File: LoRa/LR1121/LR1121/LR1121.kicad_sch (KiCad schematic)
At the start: 0 parts

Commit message: [LR1121] Add GPS in the project
GPS and power module was add in the project
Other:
- added sheet LoRa-system (LoRa-system.kicad_sch)
- note added: "Charger battery circuit."
- note added: "LR1121: DIO9, DIO8 Multi-purpose digital I/O STM32L55: PA2 UART2_TX PA3 UART2_RX PA4 SPI1_NSS PA5 SPI1_SCK PA6 SPI1_MISO PA7 SPI1_MOSI PA9 UART1_TX PA10 UART1_RX PA11 USB_DM PA12 USB_DP PB6 I2C1_SCL PB7 I2C1_SDA PB8 CAN1_TX PB9 CAN1_RX PB10 I2C2_SCL PB11 I2C2_SDA PB12 SPI2_NSS PB13 SPI2_SCK PB14 SPI2_MISO PB15 SPI2_MOSI"
- note added: "MT29F4G01ABAFDWB-IT:F TR 133 MHz clock frequency (MAX) LBAA0XV2GT: The SPI runs on the external SCK clock to allow high speed up to 16 MHz"
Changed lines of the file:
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@@
 	(generator_version "9.0")
 	(paper "A4")
+	(text "	LR1121:\nDIO9, DIO8 		Multi-purpose digital I/O\n\n	STM32L55:\n\nPA2		UART2_TX	\nPA3		UART2_RX\n\nPA4		SPI1_NSS\nPA5		SPI1_SCK\nPA6		SPI1_MISO\nPA7		SPI1_MOSI\n\nPA9		UART1_TX\nPA10	UART1_RX\n\nPA11	USB_DM\nPA12	USB_DP\n\nPB6		I2C1_SCL\nPB7		I2C1_SDA\n\nPB8		CAN1_TX\nPB9		CAN1_RX\n\nPB10	I2C2_SCL\nPB11	I2C2_SDA\n\nPB12	SPI2_NSS\nPB13	SPI2_SCK\nPB14	SPI2_MISO\nPB15	SPI2_MOSI"
+		(exclude_from_sim no)
+		(at 18.034 20.574 0)
+		(effects
+			(font
+				(size 2 2)
+			)
+			(justify left top)
+		)
+	)
+	(text "MT29F4G01ABAFDWB-IT:F TR\n\n133 MHz clock frequency (MAX)\n\n\nLBAA0XV2GT:\n\nThe SPI runs on the external SCK \nclock to allow high speed up to 16 MHz"
+		(exclude_from_sim no)
+		(at 24.638 150.622 0)
+		(effects
+			(font
+				(size 2 2)
+			)
+			(justify left top)
+		)
+	)
+	(text "Charger battery circuit."
+		(exclude_from_sim no)
+		(at 106.172 30.226 0)
+		(effects
+			(font
+				(size 2 2)
+			)
+			(justify left top)
+		)
+	)
+	(sheet
+		(at 168.275 22.225)
+		(size 87.63 125.095)
+		(exclude_from_sim no)
+		(in_bom yes)
+		(on_board yes)
+		(dnp no)
+		(fields_autoplaced yes)
+		(stroke
+			(width 0.1524)
+			(type solid)
+		)
+		(fill
+			(color 0 0 0 0.0000)
+		)
+		(property "Sheetname" "LoRa-system"
+			(at 168.275 21.1484 0)
+			(effects
+				(font
+					(size 2 2)
+				)
+				(justify left bottom)
+			)
+		)
+		(property "Sheetfile" "LoRa-system.kicad_sch"
+			(at 168.275 148.1966 0)
+			(effects
+				(font
+					(size 2 2)
+				)
+				(justify left top)
+			)
+		)
+		(instances
+			(project "LR1121"
+				(path "/6f884698-74c0-4ae2-9ae5-e4bb363c76bd"
+					(page "2")
+				)
+			)
+		)
+	)
 	(sheet_instances
 		(path "/"

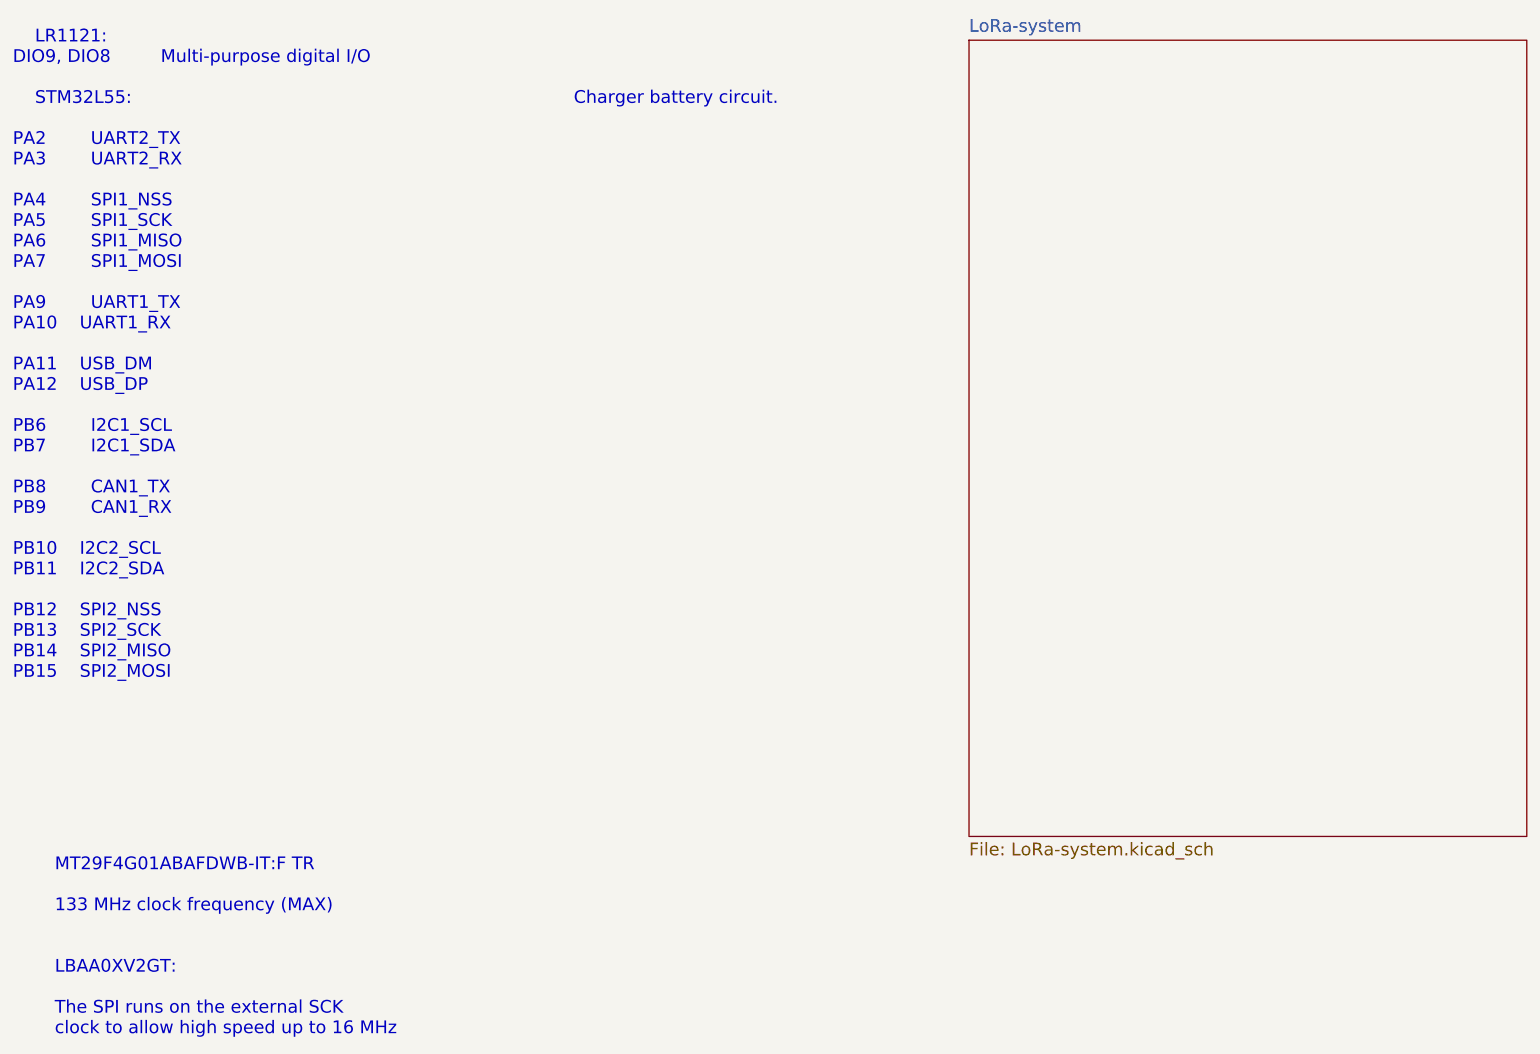
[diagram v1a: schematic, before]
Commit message: [BB_IMX8ML] Change MCU F280015x
Change MCU STM32H5 for F2800157 dual core real-time
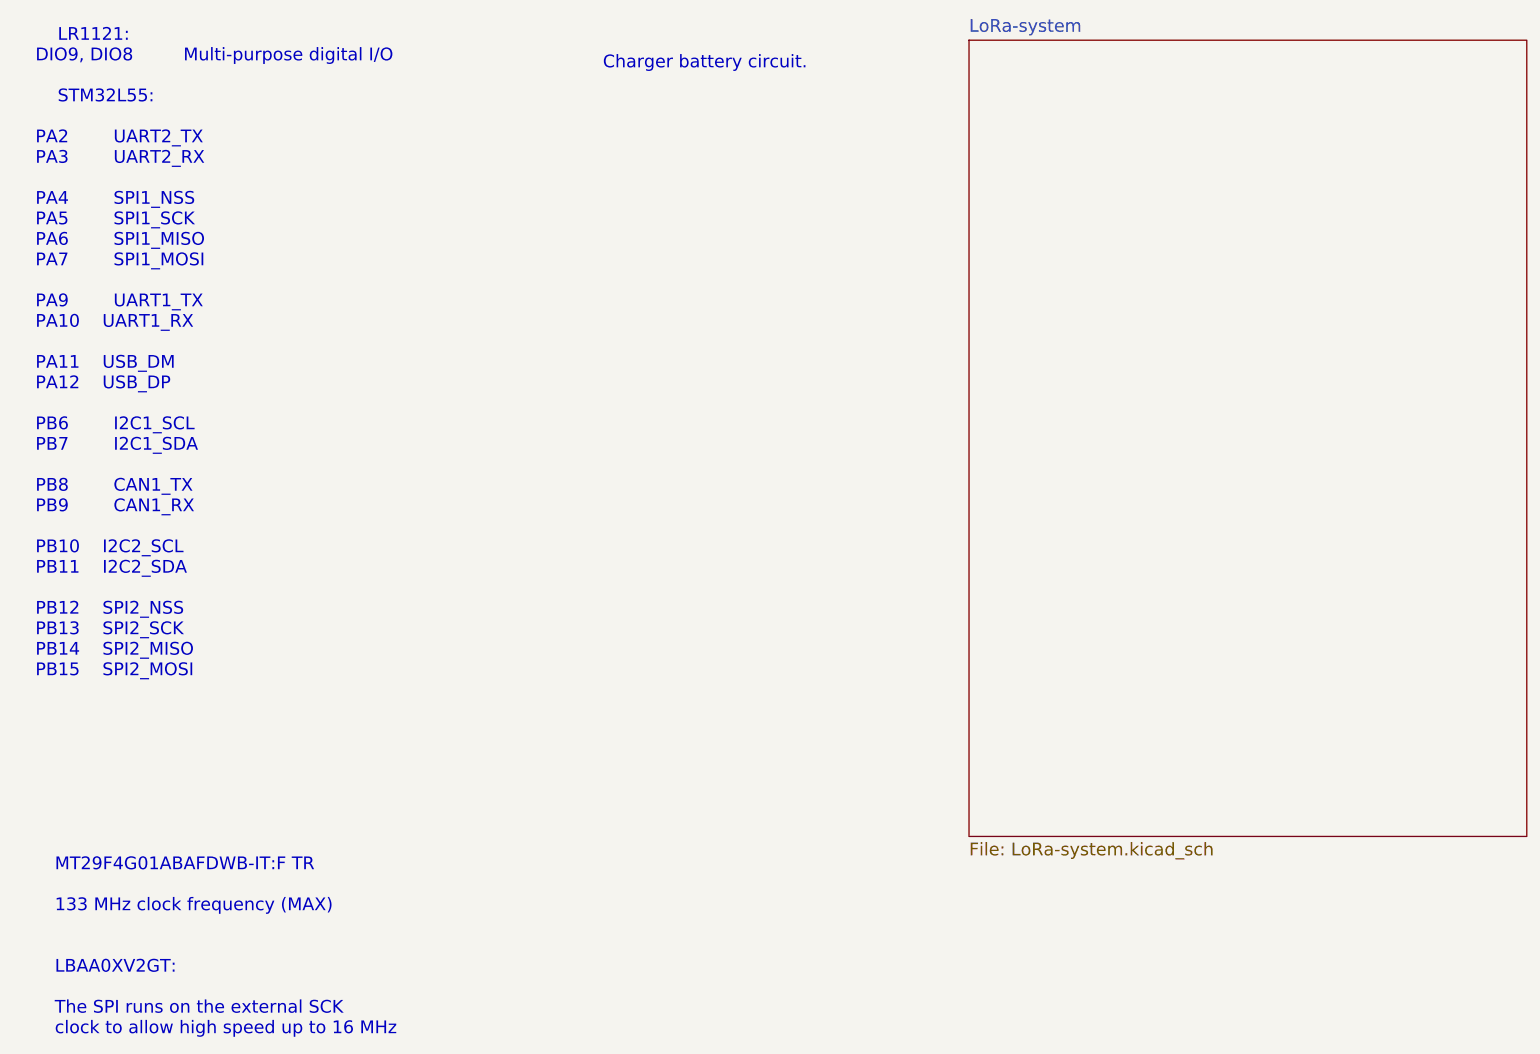
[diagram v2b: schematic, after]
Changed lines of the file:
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@@
 	(text "	LR1121:\nDIO9, DIO8 		Multi-purpose digital I/O\n\n	STM32L55:\n\nPA2		UART2_TX	\nPA3		UART2_RX\n\nPA4		SPI1_NSS\nPA5		SPI1_SCK\nPA6		SPI1_MISO\nPA7		SPI1_MOSI\n\nPA9		UART1_TX\nPA10	UART1_RX\n\nPA11	USB_DM\nPA12	USB_DP\n\nPB6		I2C1_SCL\nPB7		I2C1_SDA\n\nPB8		CAN1_TX\nPB9		CAN1_RX\n\nPB10	I2C2_SCL\nPB11	I2C2_SDA\n\nPB12	SPI2_NSS\nPB13	SPI2_SCK\nPB14	SPI2_MISO\nPB15	SPI2_MOSI"
 		(exclude_from_sim no)
-		(at 18.034 20.574 0)
+		(at 21.59 20.32 0)
 		(effects
 			(font
@@
 	(text "Charger battery circuit."
 		(exclude_from_sim no)
-		(at 106.172 30.226 0)
+		(at 110.744 24.638 0)
 		(effects
 			(font
